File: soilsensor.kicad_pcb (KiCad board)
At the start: 2 copper layers, 23 x 113 mm, 32 parts, among them J1 CONN_01X07, J2 BATT_CONN, P1 USB_OTG, Q1 Q_NMOS_GSD, Q2 Q_PMOS_GSD, Q3 Q_PMOS_GSD, U1 DS18B20U, U2 RFD77101, U3 MCP73811T, U4 AP2204K-3.0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

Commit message: update pcb
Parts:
- added G***: LOGO, LOGO, F.Cu at (105.5, 72.8)
- added R10: 1.8k, Resistors_SMD:R_0603, F.Cu at (103.7, 56.7)
- C9: footprint SoilMeasuringBoard:coil_sensor -> SoilMeasuringBoard:C_Sensor
- R2: value 3.3k -> 1.5k
- moved D2 14.9 mm to (102.0, 49.0)
- moved C4 13.3 mm to (107.0, 49.8)
- moved D1 12.7 mm to (110.2, 68.5), turned to 270 degrees
- moved U4 10.7 mm to (102.7, 52.5), turned to 270 degrees
- moved U3 9.39 mm to (97.2, 53.4), turned to 180 degrees
- moved R7 8.73 mm to (106.3, 56.7)
- moved C5 7.85 mm to (102.9, 55.2), turned to 180 degrees
- moved Q2 7.01 mm to (104.6, 49.0), turned to 270 degrees
- moved P1 5.94 mm to (96.5, 59.5)
- moved C2 5.19 mm to (96.8, 47.5), turned to 0 degrees
- moved C3 4.82 mm to (97.9, 51.0), turned to 180 degrees
- moved R2 4.81 mm to (100.2, 53.1), turned to 270 degrees
- moved Q1 4.60 mm to (106.0, 54.3), turned to 180 degrees
- moved R8 4.54 mm to (101.2, 59.0)
- moved R1 4.30 mm to (112.5, 67.9)
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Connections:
- net /CapacitiveSoilSensor/SensorOut renamed /SS_OUT
- net /CapacitiveSoilSensor/~EN renamed /~SS_EN
- J1 pad 2: (no net) -> Net-(J1-Pad2)
- P1 pad 2: (no net) -> Net-(P1-Pad2)
- P1 pad 3: (no net) -> Net-(P1-Pad3)
- P1 pad 4: (no net) -> Net-(P1-Pad4)
- Q1 pad 1: /PowerMgmt/BATT_V_EN -> /V_BATT_EN
- R2 pad 2: /PowerMgmt/BATT_V -> Net-(R10-Pad1)
- R7 pad 1: /PowerMgmt/BATT_V -> /V_BATT
- U1 pad 2: (no net) -> Net-(U1-Pad2)
- U1 pad 3: (no net) -> Net-(U1-Pad3)
- U1 pad 5: (no net) -> Net-(U1-Pad5)
- U1 pad 6: (no net) -> Net-(U1-Pad6)
- U1 pad 7: (no net) -> Net-(U1-Pad7)
- U2 pad 10: (no net) -> Net-(U2-Pad10)
- U2 pad 11: (no net) -> /V_BATT_EN
- U2 pad 12: (no net) -> Net-(U2-Pad12)
- U2 pad 13: (no net) -> Net-(U2-Pad13)
- U2 pad 14: (no net) -> Net-(U2-Pad14)
- U2 pad 15: (no net) -> Net-(U2-Pad15)
- U2 pad 16: (no net) -> Net-(U2-Pad16)
- U2 pad 17: (no net) -> Net-(U2-Pad17)
- U2 pad 18: (no net) -> Net-(U2-Pad18)
- U2 pad 20: /PowerMgmt/BATT_V_EN -> Net-(U2-Pad20)
- U2 pad 21: /PowerMgmt/BATT_V -> /V_BATT
- U2 pad 27: (no net) -> Net-(U2-Pad27)
- U2 pad 28: (no net) -> Net-(U2-Pad28)
- U2 pad 29: (no net) -> Net-(U2-Pad29)
- U2 pad 3: (no net) -> Net-(U2-Pad3)
- U2 pad 31: (no net) -> Net-(U2-Pad31)
- U2 pad 32: (no net) -> Net-(U2-Pad32)
- U2 pad 33: (no net) -> Net-(U2-Pad33)
- U2 pad 34: (no net) -> Net-(U2-Pad34)
- U2 pad 35: (no net) -> Net-(U2-Pad35)
- U2 pad 36: (no net) -> Net-(U2-Pad36)
- U2 pad 37: (no net) -> Net-(U2-Pad37)
- U2 pad 38: (no net) -> Net-(U2-Pad38)
- U2 pad 39: (no net) -> Net-(U2-Pad39)
- U2 pad 40: (no net) -> Net-(U2-Pad40)
- U2 pad 41: (no net) -> Net-(U2-Pad41)
- U2 pad 5: (no net) -> Net-(U2-Pad5)
- U4 pad 4: (no net) -> Net-(U4-Pad4)
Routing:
- net GND: track 162.1 -> 113.5 mm
- net Net-(C9-Pad1): track 18.2 -> 55.0 mm
- net /PowerMgmt/BATT_V: track 19.4 -> 0.00 mm
- net Net-(C2-Pad1): track 10.3 -> 29.4 mm
- net /PowerMgmt/BATT_V_EN: track 14.4 -> 0.00 mm
- net VDD: track 20.1 -> 30.6 mm
- net /SS_OUT: track 30.1 -> 22.1 mm
- net /V_BATT: track 0.00 -> 7.73 mm
- net Net-(R10-Pad1): track 0.00 -> 5.34 mm
- net +BATT: track 7.50 -> 12.0 mm
- net /~SS_EN: track 16.4 -> 13.0 mm
- net VBUS: track 16.7 -> 14.2 mm
- net /SWDIO/RESET: track 10.6 -> 8.40 mm
- net /GPIO1: track 20.3 -> 18.4 mm
- net Net-(R1-Pad1): track 101.7 -> 103.4 mm
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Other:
- board size 23 x 113 mm -> 21 x 113 mm

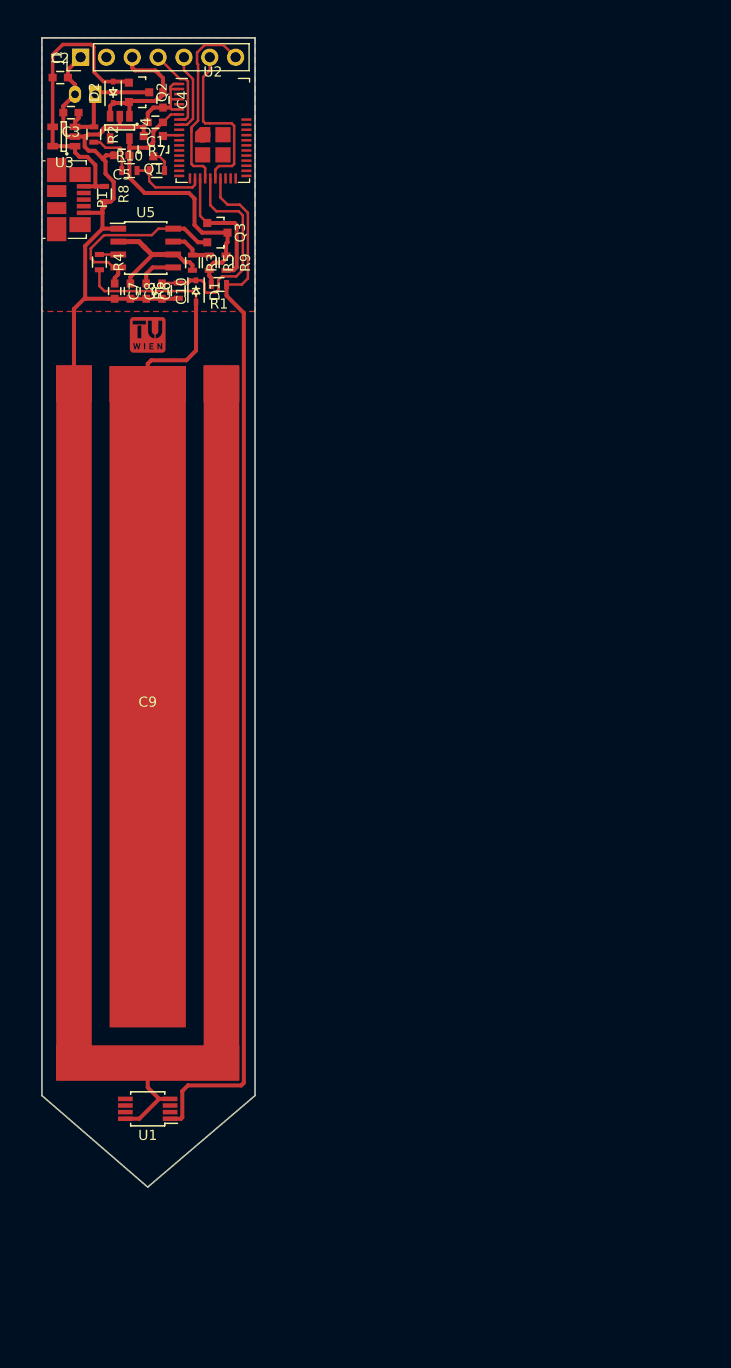
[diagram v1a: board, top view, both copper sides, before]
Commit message: fix #3: rewire p mosfet to swicht c-sensor
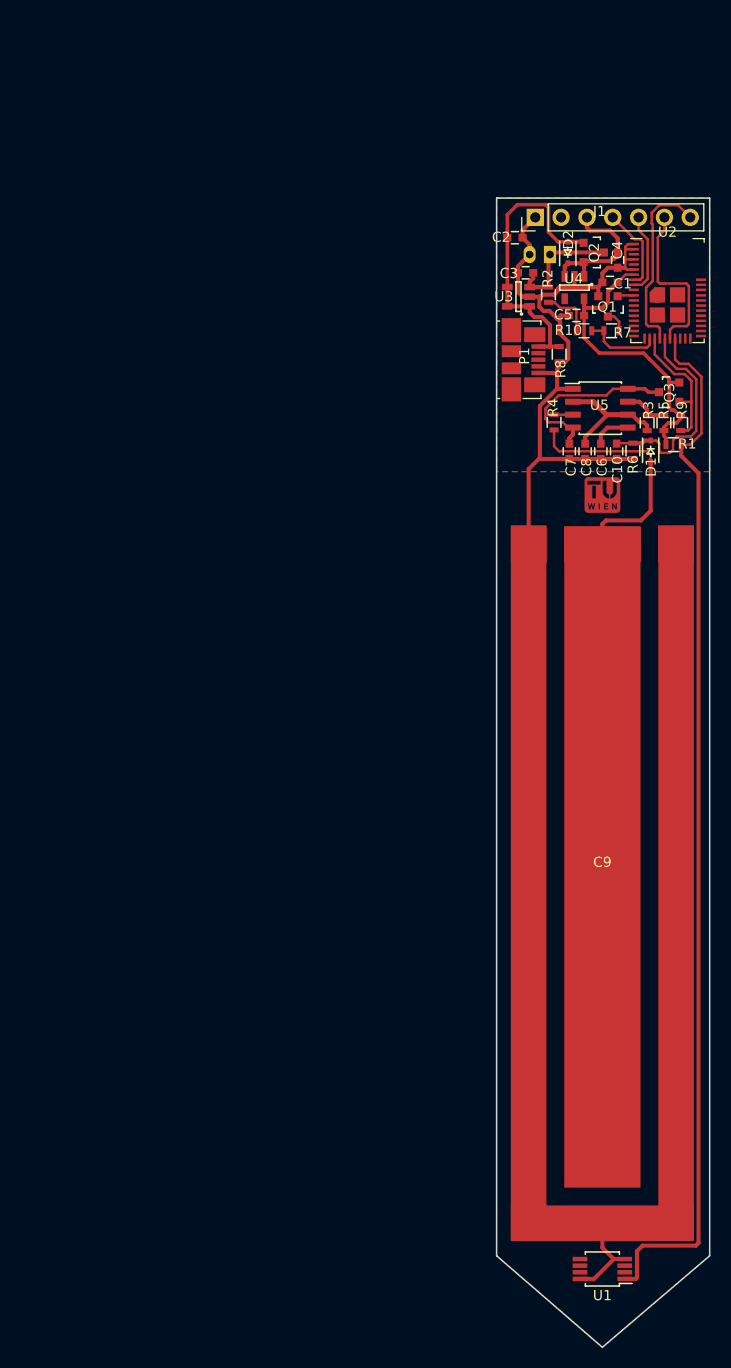
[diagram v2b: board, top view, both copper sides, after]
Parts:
- moved C10 47.4 mm to (151.6, 84.3)
- moved C2 47.4 mm to (141.6, 63.3)
- moved C3 47.4 mm to (142.6, 66.7)
- moved C5 47.4 mm to (147.6, 70.9)
- moved C8 47.4 mm to (148.5, 84.3)
- moved J1 47.4 mm to (143.6, 61.3)
- moved P1 47.4 mm to (141.2, 75.3)
- moved Q1 47.4 mm to (150.7, 70.0)
- moved Q2 47.4 mm to (149.3, 64.7)
- moved R10 47.4 mm to (148.4, 72.4)
- moved R2 47.4 mm to (144.9, 68.9)
- moved R3 47.4 mm to (154.6, 81.5)
- moved R5 47.4 mm to (156.2, 81.5)
- moved R7 47.4 mm to (151.1, 72.4)
- moved R9 47.4 mm to (157.9, 81.5)
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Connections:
- net /SS_OUT renamed /CapacitiveSoilSensor/SensorOut
- net /V_BATT renamed /PowerMgmt/BATT_V
- net /V_BATT_EN renamed /PowerMgmt/BATT_V_EN
- net /~SS_EN renamed /CapacitiveSoilSensor/~EN
- J1 pad 2: Net-(J1-Pad2) -> (no net)
- P1 pad 2: Net-(P1-Pad2) -> (no net)
- P1 pad 3: Net-(P1-Pad3) -> (no net)
- P1 pad 4: Net-(P1-Pad4) -> (no net)
- Q3 pad 2: Net-(C7-Pad1) -> VDD
- Q3 pad 3: VDD -> Net-(C7-Pad1)
- U1 pad 2: Net-(U1-Pad2) -> (no net)
- U1 pad 3: Net-(U1-Pad3) -> (no net)
- U1 pad 5: Net-(U1-Pad5) -> (no net)
- U1 pad 6: Net-(U1-Pad6) -> (no net)
- U1 pad 7: Net-(U1-Pad7) -> (no net)
- U2 pad 10: Net-(U2-Pad10) -> (no net)
- U2 pad 12: Net-(U2-Pad12) -> (no net)
- U2 pad 13: Net-(U2-Pad13) -> (no net)
- U2 pad 14: Net-(U2-Pad14) -> (no net)
- U2 pad 15: Net-(U2-Pad15) -> (no net)
- U2 pad 16: Net-(U2-Pad16) -> (no net)
- U2 pad 17: Net-(U2-Pad17) -> (no net)
- U2 pad 18: Net-(U2-Pad18) -> (no net)
- U2 pad 20: Net-(U2-Pad20) -> (no net)
- U2 pad 27: Net-(U2-Pad27) -> (no net)
- U2 pad 28: Net-(U2-Pad28) -> (no net)
- U2 pad 29: Net-(U2-Pad29) -> (no net)
- U2 pad 3: Net-(U2-Pad3) -> (no net)
- U2 pad 31: Net-(U2-Pad31) -> (no net)
- U2 pad 32: Net-(U2-Pad32) -> (no net)
- U2 pad 33: Net-(U2-Pad33) -> (no net)
- U2 pad 34: Net-(U2-Pad34) -> (no net)
- U2 pad 35: Net-(U2-Pad35) -> (no net)
- U2 pad 36: Net-(U2-Pad36) -> (no net)
- U2 pad 37: Net-(U2-Pad37) -> (no net)
- U2 pad 38: Net-(U2-Pad38) -> (no net)
- U2 pad 39: Net-(U2-Pad39) -> (no net)
- U2 pad 40: Net-(U2-Pad40) -> (no net)
- U2 pad 41: Net-(U2-Pad41) -> (no net)
- U2 pad 5: Net-(U2-Pad5) -> (no net)
- U4 pad 4: Net-(U4-Pad4) -> (no net)
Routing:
- net /CapacitiveSoilSensor/SensorOut: track 22.1 -> 21.2 mm
- net Net-(C7-Pad1): track 18.6 -> 17.9 mm
- net Net-(R1-Pad1): track 103.4 -> 102.8 mm
